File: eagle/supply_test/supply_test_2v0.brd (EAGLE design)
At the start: 25.4 x 25.4 mm, 43 parts, among them J1 JTAG_14PIN_IDC-NL, J21 AC_INFILM, Q1 2N7002, U1 TPS62122, U2 AD524, U3 MSP430FR5738

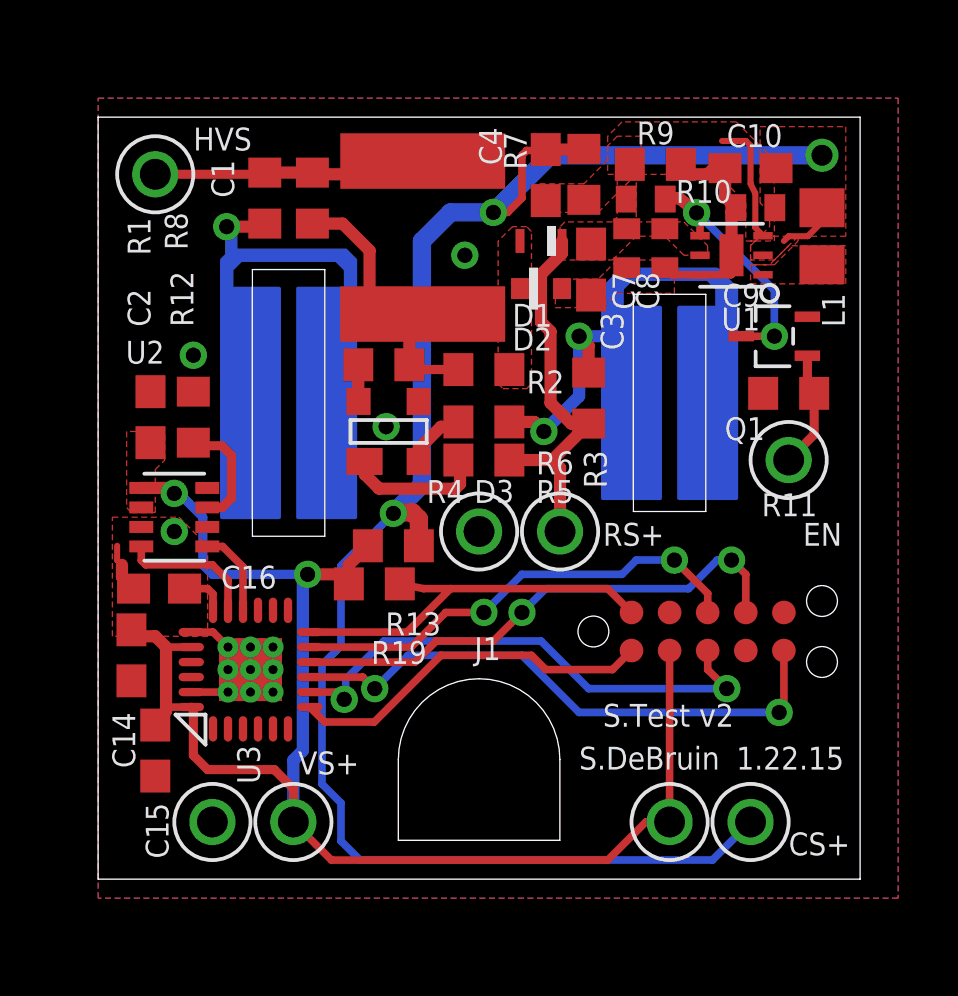
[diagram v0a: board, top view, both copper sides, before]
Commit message: finished board for supply test
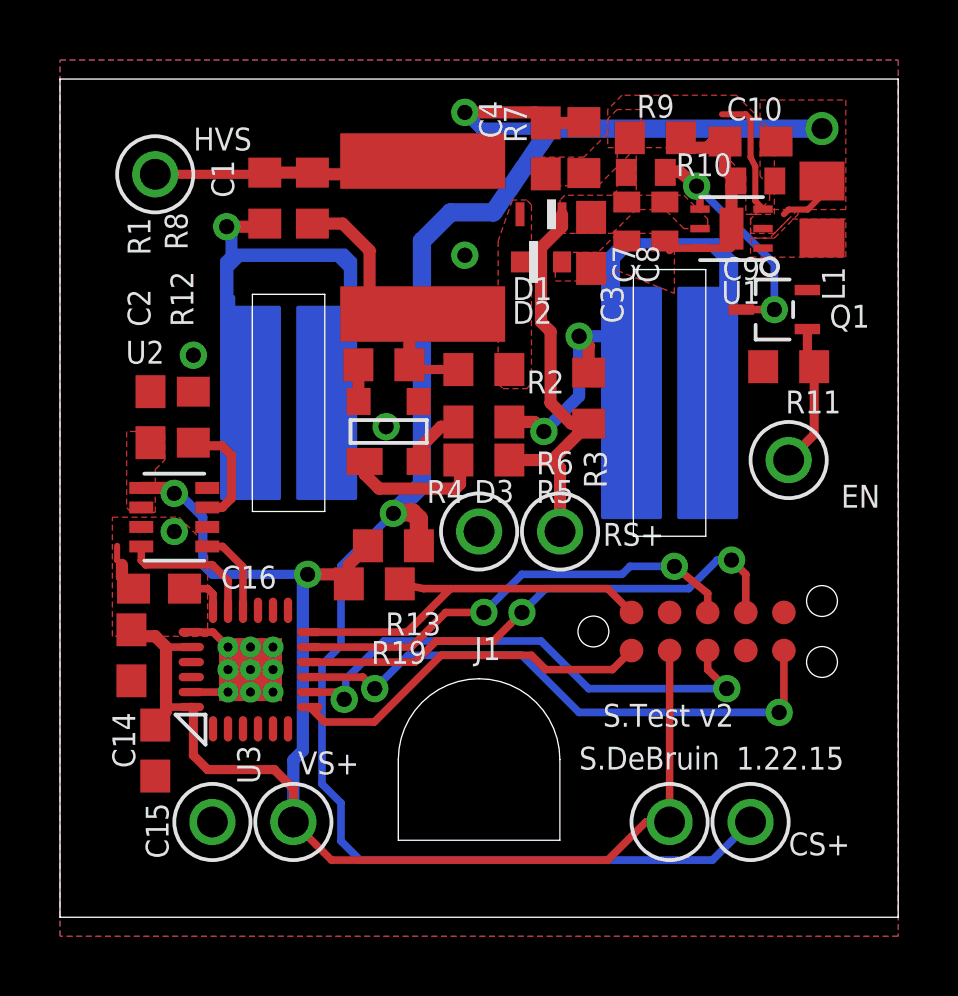
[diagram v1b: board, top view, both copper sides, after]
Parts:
- moved C7 0.89 mm to (4.92, 6.05)
- moved C8 0.89 mm to (6.19, 6.05)
- moved C9 0.89 mm to (9.21, 7.40)
- moved D1 0.89 mm to (2.06, 6.29)
- moved R10 0.89 mm to (5.56, 7.68)
- moved R7 0.89 mm to (3.49, 8.51)
- moved R9 0.89 mm to (5.87, 8.84)
- moved U1 0.89 mm to (8.41, 5.81)
- moved R11 0.89 mm to (10.3, 1.21)
- moved D2 0.89 mm to (2.06, 4.70)
- moved Q1 0.89 mm to (9.84, 3.11)
- moved C10 0.89 mm to (9.05, 8.71)
- moved C3 0.89 mm to (3.73, 5.33)
- moved C4 0.89 mm to (2.22, 8.48)
- moved L1 0.89 mm to (11.4, 6.45)
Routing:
- net N$11: track 59.2 -> 62.4 mm
- net N$6: track 16.9 -> 19.3 mm
- net PS_!EN!: track 3.92 -> 4.81 mm
- net VCC: track 13.0 -> 13.9 mm
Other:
- board size 25.4 x 25.4 mm -> 27.9 x 27.9 mm
